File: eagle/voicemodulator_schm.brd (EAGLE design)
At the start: 109 x 84 mm, 39 parts, among them T1 2N5089, T2 2N5089, T3 2N5089, T4 2N5089

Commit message: Made USB 3.0 connections
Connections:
- net 0: now also USB_3.0.2, USB_3.0.3, USB_3.0.4, USB_3.0.5, USB_3.0.6, USB_3.0.7, USB_3.0.8, USB_3.0.9, USB_3.0.S1, USB_3.0.S2
- net VCC: now also USB_3.0.1
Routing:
- net VCC: track 216.6 -> 283.9 mm, vias 6 -> 8
- net 0: track 403.9 -> 444.7 mm
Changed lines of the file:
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@@
 <layer number="43" name="vRestrict" color="2" fill="10" visible="yes" active="yes"/>
 <layer number="44" name="Drills" color="7" fill="1" visible="no" active="yes"/>
-<layer number="45" name="Holes" color="7" fill="1" visible="no" active="yes"/>
+<layer number="45" name="Holes" color="7" fill="1" visible="yes" active="yes"/>
 <layer number="46" name="Milling" color="3" fill="1" visible="no" active="yes"/>
 <layer number="47" name="Measures" color="7" fill="1" visible="no" active="yes"/>
@@
 <wire x1="40.698" y1="44" x2="40.928" y2="43.77" width="0.1524" layer="1"/>
 <wire x1="35.5" y1="43" x2="38.5" y2="43" width="0.1524" layer="1"/>
+<contactref element="USB_3.0" pad="2"/>
+<contactref element="USB_3.0" pad="3"/>
+<contactref element="USB_3.0" pad="4"/>
+<contactref element="USB_3.0" pad="7"/>
+<contactref element="USB_3.0" pad="9"/>
+<contactref element="USB_3.0" pad="6"/>
+<contactref element="USB_3.0" pad="8"/>
+<contactref element="USB_3.0" pad="5"/>
+<contactref element="USB_3.0" pad="S1"/>
+<contactref element="USB_3.0" pad="S2"/>
+<wire x1="101.5" y1="4.93" x2="102.94" y2="6.37" width="0.1524" layer="1"/>
+<wire x1="102.94" y1="6.37" x2="102.94" y2="7.5" width="0.1524" layer="1"/>
+<wire x1="102.94" y1="7.5" x2="102" y2="7.5" width="0.1524" layer="1"/>
+<wire x1="102" y1="7.5" x2="101.5" y2="8" width="0.1524" layer="1"/>
+<wire x1="102.94" y1="7.5" x2="102.94" y2="9.5" width="0.1524" layer="1"/>
+<wire x1="102.94" y1="9.5" x2="101.5" y2="9.5" width="0.1524" layer="1"/>
+<wire x1="101.5" y1="9.5" x2="101.5" y2="10.5" width="0.1524" layer="1"/>
+<wire x1="101.5" y1="10.5" x2="103" y2="10.5" width="0.1524" layer="1"/>
+<wire x1="103" y1="10.5" x2="102.94" y2="10.56" width="0.1524" layer="1"/>
+<wire x1="102.94" y1="10.56" x2="102.94" y2="11.5" width="0.1524" layer="1"/>
+<wire x1="102.94" y1="11.5" x2="102.94" y2="13.5" width="0.1524" layer="1"/>
+<wire x1="102.94" y1="13.5" x2="101.5" y2="13.5" width="0.1524" layer="1"/>
+<wire x1="101.5" y1="13.5" x2="101.5" y2="12.5" width="0.1524" layer="1"/>
+<wire x1="102.94" y1="13.5" x2="102.94" y2="15.5" width="0.1524" layer="1"/>
+<wire x1="102.94" y1="15.5" x2="102.94" y2="17.56" width="0.1524" layer="1"/>
+<wire x1="102.43" y1="18.07" x2="101.5" y2="18.07" width="0.1524" layer="1"/>
+<wire x1="102.94" y1="17.56" x2="102.43" y2="18.07" width="0.1524" layer="1"/>
+<wire x1="101.5" y1="18.07" x2="101.5" y2="35" width="0.1524" layer="1"/>
+<wire x1="101.5" y1="35" x2="103.5" y2="35" width="0.1524" layer="1"/>
 </signal>
 <signal name="N$1">
@@
 <wire x1="68.58" y1="46.99" x2="68.58" y2="52.08" width="0.1524" layer="1"/>
 <wire x1="68.58" y1="52.08" x2="69.5" y2="53" width="0.1524" layer="1"/>
+<contactref element="USB_3.0" pad="1"/>
+<wire x1="78" y1="5.54" x2="79.5" y2="7.04" width="0.1524" layer="1"/>
+<wire x1="79.5" y1="7.04" x2="79.5" y2="10.5" width="0.1524" layer="1"/>
+<wire x1="79.5" y1="10.5" x2="80.5" y2="10.5" width="0.1524" layer="1"/>
+<via x="80.5" y="10.5" extent="1-16" drill="0.35"/>
+<wire x1="80.5" y1="10.5" x2="80.5" y2="23" width="0.1524" layer="16"/>
+<wire x1="80.5" y1="23" x2="90.5" y2="33" width="0.1524" layer="16"/>
+<wire x1="90.5" y1="33" x2="90.5" y2="36" width="0.1524" layer="16"/>
+<wire x1="90.5" y1="36" x2="92.5" y2="36" width="0.1524" layer="16"/>
+<wire x1="92.5" y1="36" x2="94" y2="34.5" width="0.1524" layer="16"/>
+<wire x1="94" y1="34.5" x2="94" y2="15" width="0.1524" layer="16"/>
+<via x="94" y="15" extent="1-16" drill="0.35"/>
+<wire x1="94" y1="15" x2="101.5" y2="15" width="0.1524" layer="1"/>
 </signal>
 <signal name="N$2">

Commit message: Added name of LEDs and labeling for group/project on silk screen layer
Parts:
- renumbered LED1 to ADC_POWER, LED2 to DAC_POWER, LED3 to AMEGA_POWER
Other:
- board text added: "ECE 411"
- board text added: "Team 6"
- board text added: "Voice Modulator"
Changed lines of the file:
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@@
 <wire x1="107.72" y1="83.99" x2="0" y2="83.49" width="0" layer="20"/>
 <wire x1="0" y1="83.49" x2="0" y2="0" width="0" layer="20"/>
+<text x="84" y="13.5" size="1.778" layer="25">Team 6 </text>
+<text x="83.5" y="7.5" size="1.778" layer="25">Voice
+Modulator</text>
+<text x="83.5" y="17" size="1.778" layer="25">ECE 411</text>
 </plain>
 <attributes>
@@
 <attribute name="VALUE" x="44.452" y="16.1044" size="1.27" layer="27"/>
 </element>
-<element name="LED1" library="led" library_urn="urn:adsk.eagle:library:259" package="LED10MM" package3d_urn="urn:adsk.eagle:package:15828/1" value="" x="84.5" y="75.5">
+<element name="ADC_POWER" library="led" library_urn="urn:adsk.eagle:library:259" package="LED10MM" package3d_urn="urn:adsk.eagle:package:15828/1" value="" x="84.5" y="75.5">
 <attribute name="NAME" x="90.85" y="76.77" size="1.27" layer="25"/>
 <attribute name="VALUE" x="90.85" y="74.23" size="1.27" layer="27"/>
 </element>
-<element name="LED2" library="led" library_urn="urn:adsk.eagle:library:259" package="LED10MM" package3d_urn="urn:adsk.eagle:package:15828/1" value="" x="85" y="62">
+<element name="DAC_POWER" library="led" library_urn="urn:adsk.eagle:library:259" package="LED10MM" package3d_urn="urn:adsk.eagle:package:15828/1" value="" x="85" y="62">
 <attribute name="NAME" x="91.35" y="63.27" size="1.27" layer="25"/>
 <attribute name="VALUE" x="91.35" y="60.73" size="1.27" layer="27"/>
 </element>
-<element name="LED3" library="led" library_urn="urn:adsk.eagle:library:259" package="LED10MM" package3d_urn="urn:adsk.eagle:package:15828/1" value="" x="85" y="48.5">
+<element name="AMEGA_POWER" library="led" library_urn="urn:adsk.eagle:library:259" package="LED10MM" package3d_urn="urn:adsk.eagle:package:15828/1" value="" x="85" y="48.5">
 <attribute name="NAME" x="91.35" y="49.77" size="1.27" layer="25"/>
 <attribute name="VALUE" x="91.35" y="47.23" size="1.27" layer="27"/>
@@
 <wire x1="43" y1="19" x2="42.5" y2="19.5" width="0.1524" layer="1"/>
 <wire x1="42.5" y1="19.5" x2="42.5" y2="22.5" width="0.1524" layer="1"/>
-<contactref element="LED1" pad="A"/>
-<contactref element="LED2" pad="A"/>
-<contactref element="LED2" pad="K"/>
+<contactref element="ADC_POWER" pad="A"/>
+<contactref element="DAC_POWER" pad="A"/>
+<contactref element="DAC_POWER" pad="K"/>
 <contactref element="DAC" pad="1"/>
 <contactref element="DAC" pad="6"/>
-<contactref element="LED3" pad="A"/>
+<contactref element="AMEGA_POWER" pad="A"/>
 <wire x1="83.73" y1="48.5" x2="83.73" y2="44.73" width="0.1524" layer="1"/>
 <wire x1="80.91" y1="41.91" x2="78" y2="41.91" width="0.1524" layer="1"/>
@@
 <contactref element="ADC" pad="VDD"/>
 <wire x1="55.88" y1="71.12" x2="53.34" y2="71.12" width="0.1524" layer="1"/>
-<contactref element="LED1" pad="K"/>
+<contactref element="ADC_POWER" pad="K"/>
 <wire x1="53.34" y1="71.12" x2="53.34" y2="68.66" width="0.1524" layer="1"/>
 <wire x1="53.34" y1="68.66" x2="53.5" y2="68.5" width="0.1524" layer="1"/>
@@
 </signal>
 <signal name="N$21">
-<contactref element="LED3" pad="K"/>
+<contactref element="AMEGA_POWER" pad="K"/>
 <via x="80" y="24" extent="1-16" drill="0.35"/>
 <wire x1="80" y1="24" x2="80" y2="26.5" width="0.1524" layer="16"/>
@@
 </drawing>
 <compatibility>
+<note version="6.3" minversion="6.2.2" severity="warning">
+Since Version 6.2.2 text objects can contain more than one line,
+which will not be processed correctly with this version.
+</note>
 <note version="8.2" severity="warning">
 Since Version 8.2, EAGLE supports online libraries. The ids

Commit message: Grounded LEDs on power pins, added bypass caps at power pins
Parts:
- added C5, C6, C7: 10nF, SparkFun-Capacitors:0603
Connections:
- removed net 0: ADC.AGND, ADC.DGND, C2.2, C4.2, DAC.5, DAC.7, IC1.21, IC1.22, IC1.7, ISP.1, MIC_JACK.1, MIC_JACK1.1, R10.1, R12.2, R13.1, R2.1, R3.1, R5.2, R6.1, R9.1, USB_3.0.2, USB_3.0.3, USB_3.0.4, USB_3.0.5, USB_3.0.6, USB_3.0.7, USB_3.0.8, USB_3.0.9, USB_3.0.S1, USB_3.0.S2
- new net GND: ADC.AGND, ADC.DGND, ADC_POWER.K, AMEGA_POWER.K, C2.2, C4.2, C6.2, DAC.5, DAC.6, DAC.7, DAC_POWER.A, DAC_POWER.K, IC1.21, IC1.22, IC1.7, ISP.1, MIC_JACK.1, MIC_JACK1.1, R10.1, R12.2, R13.1, R2.1, R3.1, R5.2, R6.1, R9.1, USB_3.0.2, USB_3.0.3, USB_3.0.4, USB_3.0.5, USB_3.0.6, USB_3.0.7, USB_3.0.8, USB_3.0.9, USB_3.0.S1, USB_3.0.S2
- new net N$25: C5.2, IC1.8
- net N$18: now also C6.1, DAC.1; no longer ADC.VDD, ADC.VREF, ADC_POWER.K
- net N$21: now also ADC.VDD, C7.1; no longer AMEGA_POWER.K, IC1.20, IC1.8
- net VCC: now also ADC.VREF, C5.1, C7.2, IC1.20; no longer DAC.1, DAC.6, DAC_POWER.A, DAC_POWER.K
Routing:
- net GND: track 0.00 -> 495.8 mm, vias 0 -> 15
- net 0: track 444.7 -> 0.00 mm, vias 13 -> 0
- net VCC: track 283.9 -> 412.7 mm, vias 8 -> 18
- net N$21: track 116.9 -> 12.7 mm, vias 6 -> 0
- net N$25: track 0.00 -> 62.6 mm, vias 0 -> 6
- net N$18: track 42.0 -> 20.7 mm, vias 0 -> 2

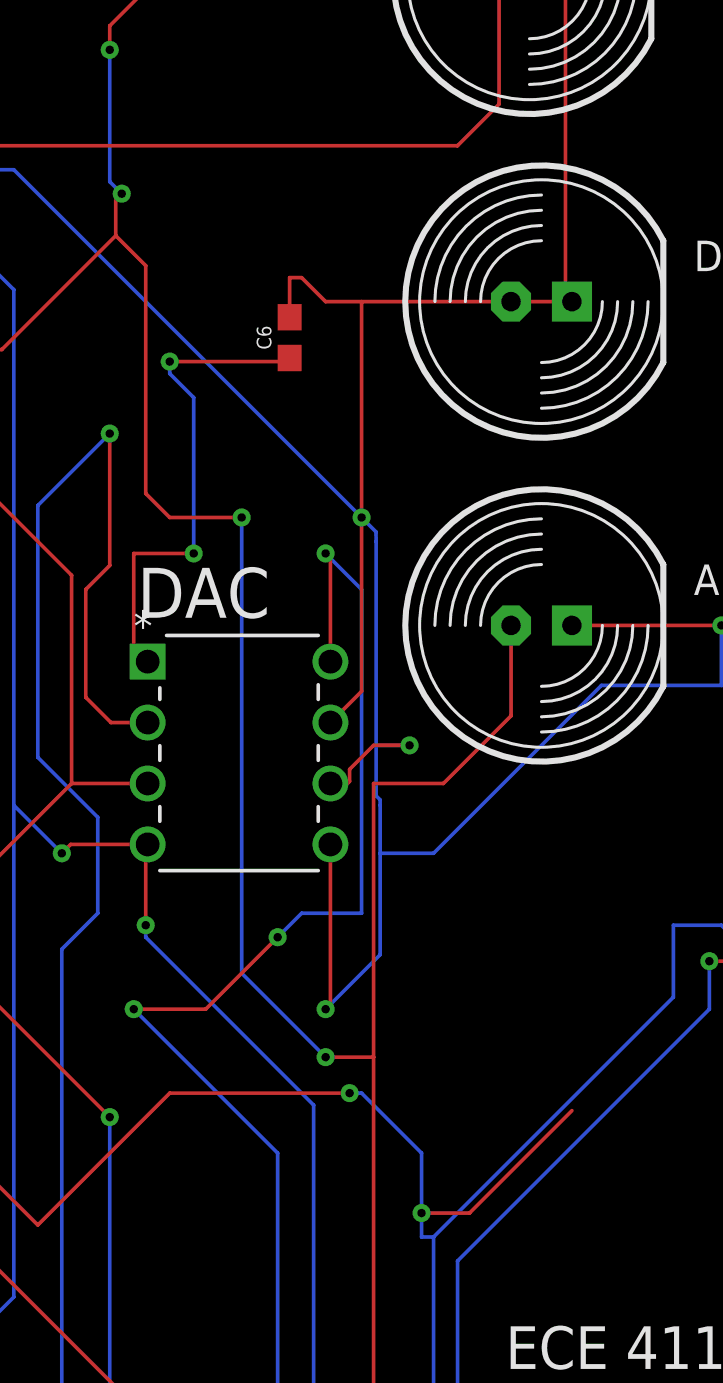
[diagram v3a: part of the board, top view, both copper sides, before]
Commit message: Fixed erc error I missed on DAC
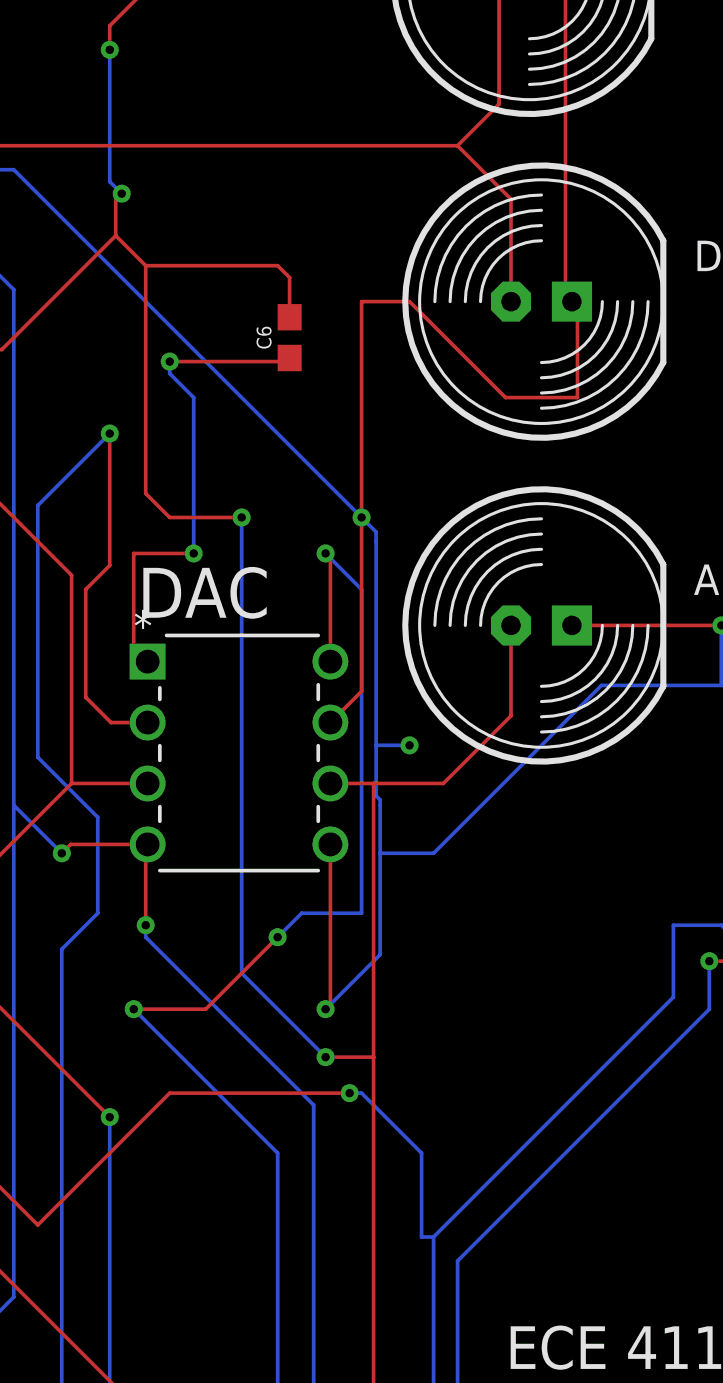
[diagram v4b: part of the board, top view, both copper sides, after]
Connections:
- net GND: no longer C6.2, DAC.6, DAC_POWER.A
- net VCC: now also C6.2, DAC.6, DAC_POWER.A
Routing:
- net VCC: track 412.7 -> 421.8 mm, vias 18 -> 17
- net GND: track 495.8 -> 492.7 mm
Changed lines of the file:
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@@
 <contactref element="AMEGA_POWER" pad="K"/>
 <contactref element="ADC_POWER" pad="K"/>
-<contactref element="DAC_POWER" pad="A"/>
 <contactref element="DAC_POWER" pad="K"/>
-<contactref element="DAC" pad="6"/>
 <wire x1="86.27" y1="62" x2="86" y2="62" width="0.1524" layer="1"/>
-<contactref element="C6" pad="2"/>
-<wire x1="86" y1="62" x2="83.73" y2="62" width="0.1524" layer="1"/>
 <wire x1="85.77" y1="75.5" x2="86" y2="75.27" width="0.1524" layer="1"/>
 <wire x1="86" y1="75.27" x2="86" y2="62" width="0.1524" layer="1"/>
-<wire x1="83.73" y1="62" x2="77.5" y2="62" width="0.1524" layer="1"/>
-<wire x1="77.5" y1="62" x2="76" y2="62" width="0.1524" layer="1"/>
-<wire x1="76" y1="62" x2="75" y2="63" width="0.1524" layer="1"/>
-<wire x1="75" y1="63" x2="74.5" y2="63" width="0.1524" layer="1"/>
-<wire x1="74.5" y1="63" x2="74.5" y2="61.35" width="0.1524" layer="1"/>
 <wire x1="77.5" y1="53" x2="77.5" y2="62" width="0.1524" layer="1"/>
 <wire x1="86.27" y1="48.5" x2="92.5" y2="48.5" width="0.1524" layer="1"/>
@@
 <wire x1="78.106771875" y1="43.5" x2="79.5" y2="43.5" width="0.1524" layer="16"/>
 <via x="79.5" y="43.5" extent="1-16" drill="0.35"/>
-<wire x1="79.5" y1="43.5" x2="78" y2="43.5" width="0.1524" layer="1"/>
-<wire x1="78" y1="43.5" x2="77" y2="42.5" width="0.1524" layer="1"/>
-<wire x1="77" y1="42.5" x2="77" y2="42" width="0.1524" layer="1"/>
-<wire x1="77" y1="42" x2="76.91" y2="41.91" width="0.1524" layer="1"/>
-<wire x1="76.91" y1="41.91" x2="76.2" y2="41.91" width="0.1524" layer="1"/>
+<wire x1="77.5" y1="62" x2="79.5" y2="62" width="0.1524" layer="1"/>
+<wire x1="79.5" y1="62" x2="83.5" y2="58" width="0.1524" layer="1"/>
+<wire x1="83.5" y1="58" x2="86.5" y2="58" width="0.1524" layer="1"/>
+<wire x1="86.5" y1="58" x2="86.5" y2="61.77" width="0.1524" layer="1"/>
+<wire x1="86.5" y1="61.77" x2="86.27" y2="62" width="0.1524" layer="1"/>
 </signal>
 <signal name="N$1">
@@
 <contactref element="IC1" pad="20"/>
 <contactref element="C5" pad="1"/>
-<via x="80" y="24" extent="1-16" drill="0.35"/>
-<wire x1="80" y1="24" x2="80" y2="26.5" width="0.1524" layer="16"/>
 <wire x1="80" y1="26.5" x2="77.5" y2="29" width="0.1524" layer="16"/>
 <wire x1="77.5" y1="29" x2="77" y2="29" width="0.1524" layer="16"/>
@@
 <via x="57" y="30.5" extent="1-16" drill="0.35"/>
 <wire x1="57" y1="30.5" x2="58.5" y2="30.5" width="0.1524" layer="1"/>
-<wire x1="80" y1="24" x2="82" y2="24" width="0.1524" layer="1"/>
-<wire x1="82" y1="24" x2="86.27" y2="28.27" width="0.1524" layer="1"/>
 <wire x1="54.00894375" y1="37" x2="53" y2="38.00894375" width="0.1524" layer="1"/>
 <wire x1="53" y1="38.00894375" x2="53" y2="38.5" width="0.1524" layer="1"/>
@@
 <wire x1="30.5" y1="50.5" x2="30.5" y2="51.65" width="0.1524" layer="1"/>
 <wire x1="80.5" y1="23" x2="80" y2="23" width="0.1524" layer="16"/>
-<wire x1="80" y1="23" x2="80" y2="24" width="0.1524" layer="16"/>
+<contactref element="DAC_POWER" pad="A"/>
+<contactref element="DAC" pad="6"/>
+<contactref element="C6" pad="2"/>
+<wire x1="83.73" y1="62" x2="83.73" y2="66.27" width="0.1524" layer="1"/>
+<wire x1="83.73" y1="66.27" x2="81.5" y2="68.5" width="0.1524" layer="1"/>
+<wire x1="68.5" y1="63.5" x2="74" y2="63.5" width="0.1524" layer="1"/>
+<wire x1="74" y1="63.5" x2="74.5" y2="63" width="0.1524" layer="1"/>
+<wire x1="74.5" y1="63" x2="74.5" y2="61.35" width="0.1524" layer="1"/>
+<wire x1="78" y1="41.91" x2="76.2" y2="41.91" width="0.1524" layer="1"/>
+<wire x1="80" y1="23" x2="80" y2="26.5" width="0.1524" layer="16"/>
 </signal>
 <signal name="N$2">

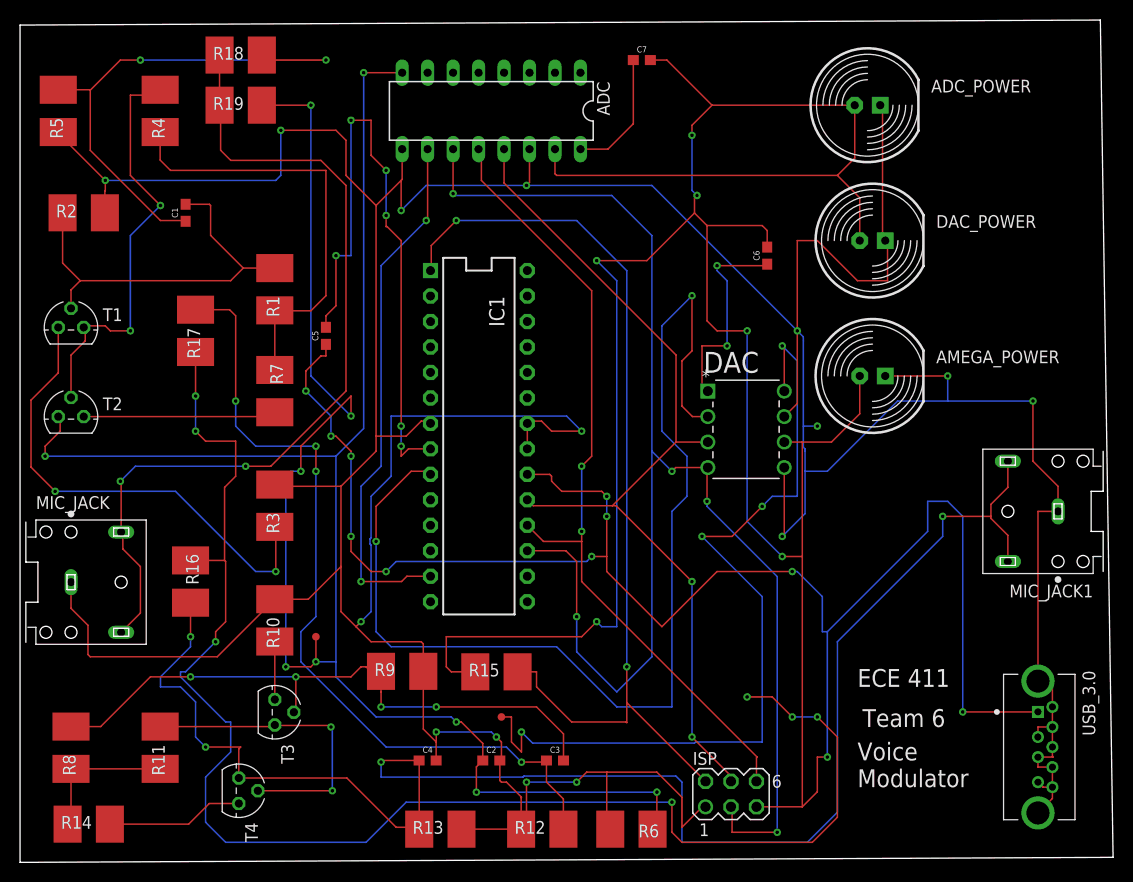
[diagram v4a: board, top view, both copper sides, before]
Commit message: Updated trace width to 0.254
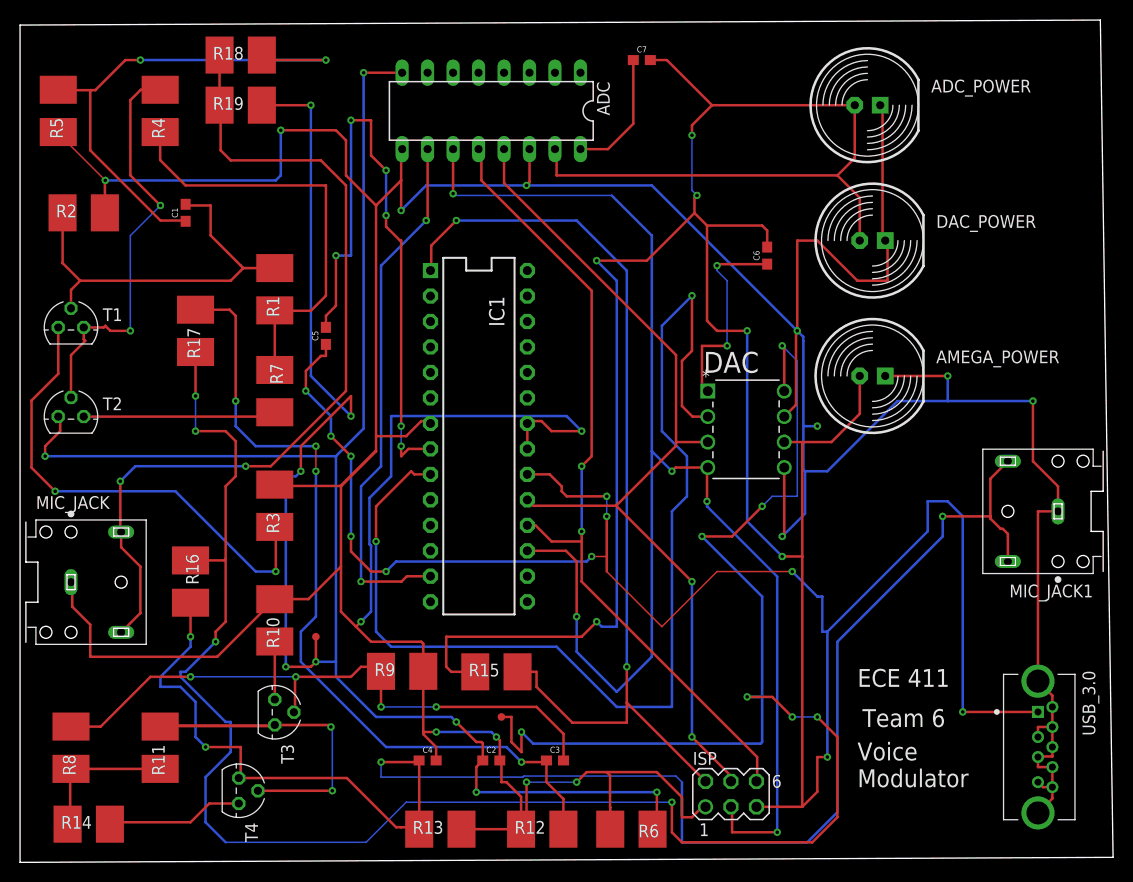
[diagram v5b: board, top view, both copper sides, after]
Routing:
- net N$14: track 31.1 -> 48.3 mm
- net N$11: track 160.7 -> 166.7 mm
- net GND: track 492.7 -> 495.8 mm
- net N$15: track 14.7 -> 16.2 mm
- net N$10: track 43.9 -> 43.1 mm
